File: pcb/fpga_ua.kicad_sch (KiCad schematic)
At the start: 15 parts

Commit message: maybe finished schematic
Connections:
- net FPGA_DEBUG_LED_BLOCK15_1: now reaches U?.C11 (IO_L11P_T1_SRCC_15)
- net FPGA_DEBUG_LED_BLOCK14_1: now reaches U?.R5 (IO_L23P_T3_A03_D19_14)
- no-connect marks 0 -> 39
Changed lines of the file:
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@@
 (kicad_sch (version 20211123) (generator eeschema)
   (paper "A4")
+  (junction (at 74.93 24.13) (diameter 0) (color 0 0 0 0)
+  )
   (junction (at 250.19 31.75) (diameter 0) (color 0 0 0 0)
   )
@@
   (junction (at 222.25 60.96) (diameter 0) (color 0 0 0 0)
   )
-  (junction (at 64.77 30.48) (diameter 0) (color 0 0 0 0)
-  )
-  (junction (at 72.39 30.48) (diameter 0) (color 0 0 0 0)
-  )
-  (junction (at 69.85 30.48) (diameter 0) (color 0 0 0 0)
+  (junction (at 64.77 24.13) (diameter 0) (color 0 0 0 0)
+  )
+  (junction (at 72.39 24.13) (diameter 0) (color 0 0 0 0)
+  )
+  (junction (at 69.85 24.13) (diameter 0) (color 0 0 0 0)
   )
   (junction (at 140.97 30.48) (diameter 0) (color 0 0 0 0)
@@
   (junction (at 143.51 30.48) (diameter 0) (color 0 0 0 0)
   )
-  (junction (at 74.93 30.48) (diameter 0) (color 0 0 0 0)
-  )
   (junction (at 213.36 31.75) (diameter 0) (color 0 0 0 0)
   )
@@
   (junction (at 222.25 24.13) (diameter 0) (color 0 0 0 0)
   )
-  (junction (at 67.31 30.48) (diameter 0) (color 0 0 0 0)
+  (junction (at 67.31 24.13) (diameter 0) (color 0 0 0 0)
   )
   (junction (at 138.43 30.48) (diameter 0) (color 0 0 0 0)
@@
   (junction (at 205.74 53.34) (diameter 0) (color 0 0 0 0)
   )
+  (no_connect (at 153.67 132.08))
+  (no_connect (at 153.67 134.62))
+  (no_connect (at 153.67 137.16))
+  (no_connect (at 153.67 139.7))
+  (no_connect (at 153.67 142.24))
+  (no_connect (at 153.67 144.78))
+  (no_connect (at 153.67 147.32))
+  (no_connect (at 153.67 149.86))
+  (no_connect (at 153.67 152.4))
+  (no_connect (at 153.67 154.94))
+  (no_connect (at 153.67 157.48))
+  (no_connect (at 153.67 50.8))
+  (no_connect (at 153.67 93.98))
+  (no_connect (at 153.67 101.6))
+  (no_connect (at 153.67 106.68))
+  (no_connect (at 153.67 109.22))
+  (no_connect (at 153.67 111.76))
+  (no_connect (at 153.67 114.3))
+  (no_connect (at 153.67 116.84))
+  (no_connect (at 153.67 119.38))
+  (no_connect (at 153.67 121.92))
+  (no_connect (at 153.67 124.46))
+  (no_connect (at 153.67 127))
+  (no_connect (at 52.07 162.56))
+  (no_connect (at 52.07 167.64))
+  (no_connect (at 52.07 170.18))
+  (no_connect (at 52.07 172.72))
+  (no_connect (at 52.07 175.26))
+  (no_connect (at 52.07 104.14))
+  (no_connect (at 52.07 147.32))
+  (no_connect (at 52.07 50.8))
+  (no_connect (at 153.67 175.26))
+  (no_connect (at 153.67 172.72))
+  (no_connect (at 153.67 160.02))
+  (no_connect (at 153.67 162.56))
+  (no_connect (at 153.67 165.1))
+  (no_connect (at 153.67 167.64))
+  (no_connect (at 153.67 170.18))
+  (no_connect (at 153.67 129.54))
   (wire (pts (xy 194.31 53.34) (xy 205.74 53.34))
     (stroke (width 0) (type default) (color 0 0 0 0))
@@
     (stroke (width 0) (type default) (color 0 0 0 0))
   )
+  (wire (pts (xy 74.93 30.48) (xy 74.93 24.13))
+    (stroke (width 0) (type default) (color 0 0 0 0))
+  )
   (wire (pts (xy 138.43 30.48) (xy 140.97 30.48))
     (stroke (width 0) (type default) (color 0 0 0 0))
@@
     (stroke (width 0) (type default) (color 0 0 0 0))
   )
+  (wire (pts (xy 64.77 24.13) (xy 64.77 30.48))
+    (stroke (width 0) (type default) (color 0 0 0 0))
+  )
   (wire (pts (xy 133.35 30.48) (xy 135.89 30.48))
     (stroke (width 0) (type default) (color 0 0 0 0))
   )
-  (wire (pts (xy 67.31 30.48) (xy 69.85 30.48))
-    (stroke (width 0) (type default) (color 0 0 0 0))
-  )
-  (wire (pts (xy 74.93 30.48) (xy 74.93 24.13))
+  (wire (pts (xy 67.31 24.13) (xy 69.85 24.13))
+    (stroke (width 0) (type default) (color 0 0 0 0))
+  )
+  (wire (pts (xy 72.39 24.13) (xy 72.39 30.48))
     (stroke (width 0) (type default) (color 0 0 0 0))
   )
@@
     (stroke (width 0) (type default) (color 0 0 0 0))
   )
+  (wire (pts (xy 69.85 24.13) (xy 69.85 30.48))
+    (stroke (width 0) (type default) (color 0 0 0 0))
+  )
   (wire (pts (xy 231.14 24.13) (xy 222.25 24.13))
     (stroke (width 0) (type default) (color 0 0 0 0))
   )
-  (wire (pts (xy 69.85 30.48) (xy 72.39 30.48))
-    (stroke (width 0) (type default) (color 0 0 0 0))
-  )
-  (wire (pts (xy 72.39 30.48) (xy 74.93 30.48))
+  (wire (pts (xy 69.85 24.13) (xy 72.39 24.13))
+    (stroke (width 0) (type default) (color 0 0 0 0))
+  )
+  (wire (pts (xy 72.39 24.13) (xy 74.93 24.13))
     (stroke (width 0) (type default) (color 0 0 0 0))
   )
@@
     (stroke (width 0) (type default) (color 0 0 0 0))
   )
-  (wire (pts (xy 153.67 104.14) (xy 163.83 104.14))
-    (stroke (width 0) (type default) (color 0 0 0 0))
-  )
   (wire (pts (xy 213.36 60.96) (xy 222.25 60.96))
     (stroke (width 0) (type default) (color 0 0 0 0))
@@
     (stroke (width 0) (type default) (color 0 0 0 0))
   )
-  (wire (pts (xy 64.77 30.48) (xy 67.31 30.48))
-    (stroke (width 0) (type default) (color 0 0 0 0))
-  )
-  (wire (pts (xy 62.23 30.48) (xy 64.77 30.48))
+  (wire (pts (xy 64.77 24.13) (xy 67.31 24.13))
+    (stroke (width 0) (type default) (color 0 0 0 0))
+  )
+  (wire (pts (xy 62.23 24.13) (xy 64.77 24.13))
     (stroke (width 0) (type default) (color 0 0 0 0))
   )
@@
     (stroke (width 0) (type default) (color 0 0 0 0))
   )
+  (wire (pts (xy 62.23 24.13) (xy 62.23 30.48))
+    (stroke (width 0) (type default) (color 0 0 0 0))
+  )
+  (wire (pts (xy 67.31 24.13) (xy 67.31 30.48))
+    (stroke (width 0) (type default) (color 0 0 0 0))
+  )
   (wire (pts (xy 213.36 24.13) (xy 205.74 24.13))
     (stroke (width 0) (type default) (color 0 0 0 0))
@@
     )
   )
+  (global_label "FPGA_DEBUG_LED_BLOCK14_1" (shape input) (at 52.07 165.1 180) (fields_autoplaced)
+    (effects (font (size 1.27 1.27)) (justify right))
+    (property "Intersheet References" "${INTERSHEET_REFS}" (id 0) (at 21.5355 165.0206 0)
+      (effects (font (size 1.27 1.27)) (justify right) hide)
+    )
+  )
   (global_label "SRAM_#CE" (shape bidirectional) (at 52.07 149.86 180) (fields_autoplaced)
     (effects (font (size 1 1)) (justify right))
@@
     (property "Intersheet References" "${INTERSHEET_REFS}" (id 0) (at 160.7605 76.1375 0)
       (effects (font (size 1 1)) (justify left) hide)
+    )
+  )
+  (global_label "FPGA_DEBUG_LED_BLOCK15_1" (shape input) (at 153.67 104.14 0) (fields_autoplaced)
+    (effects (font (size 1.27 1.27)) (justify left))
+    (property "Intersheet References" "${INTERSHEET_REFS}" (id 0) (at 184.2045 104.0606 0)
+      (effects (font (size 1.27 1.27)) (justify left) hide)
     )
   )
@@
   )
   (symbol (lib_id "FPGA_Xilinx_Artix7:XC7A100T-FTG256") (at 102.87 104.14 0) (unit 1)
-    (in_bom yes) (on_board yes) (fields_autoplaced)
-    (property "Reference" "U?" (id 0) (at 104.1401 179.07 90)
+    (in_bom yes) (on_board yes)
+    (property "Reference" "U?" (id 0) (at 107.95 179.07 0)
       (effects (font (size 1.27 1.27)) (justify right))
     )
-    (property "Value" "XC7A100T-FTG256" (id 1) (at 101.6001 179.07 90)
+    (property "Value" "XC7A100T-FTG256" (id 1) (at 101.6001 179.07 0)
       (effects (font (size 1.27 1.27)) (justify right))
     )

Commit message: everything except crystal
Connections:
- net SRAM_D0: now also U?.N13 (IO_L11P_T1_SRCC_14); no longer U?.P13 (IO_L11N_T1_SRCC_14)
- net SRAM_D1: now also U?.P13 (IO_L11N_T1_SRCC_14); no longer U?.N14 (IO_L12P_T1_MRCC_14)
- net SRAM_D2: now also U?.N14 (IO_L12P_T1_MRCC_14); no longer U?.P14 (IO_L12N_T1_MRCC_14)
- net SRAM_D3: now also U?.P14 (IO_L12N_T1_MRCC_14); no longer U?.N11 (IO_L13P_T2_MRCC_14)
- new net Oscillator Clock: U?.N11 (IO_L13P_T2_MRCC_14)

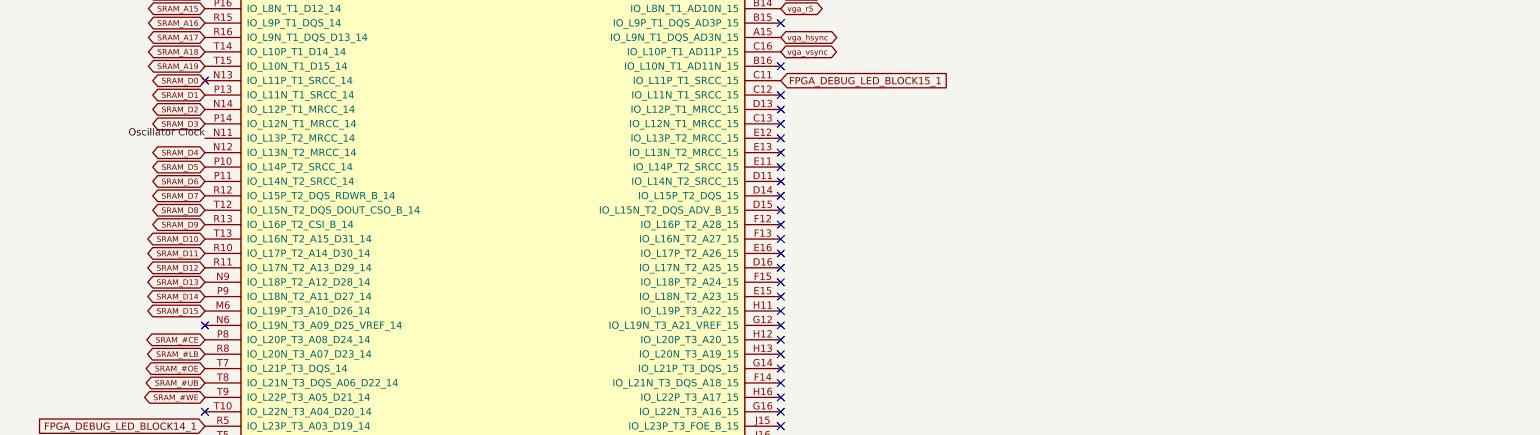
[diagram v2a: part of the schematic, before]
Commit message: add oscilattor + spi debug+ cap on sramd
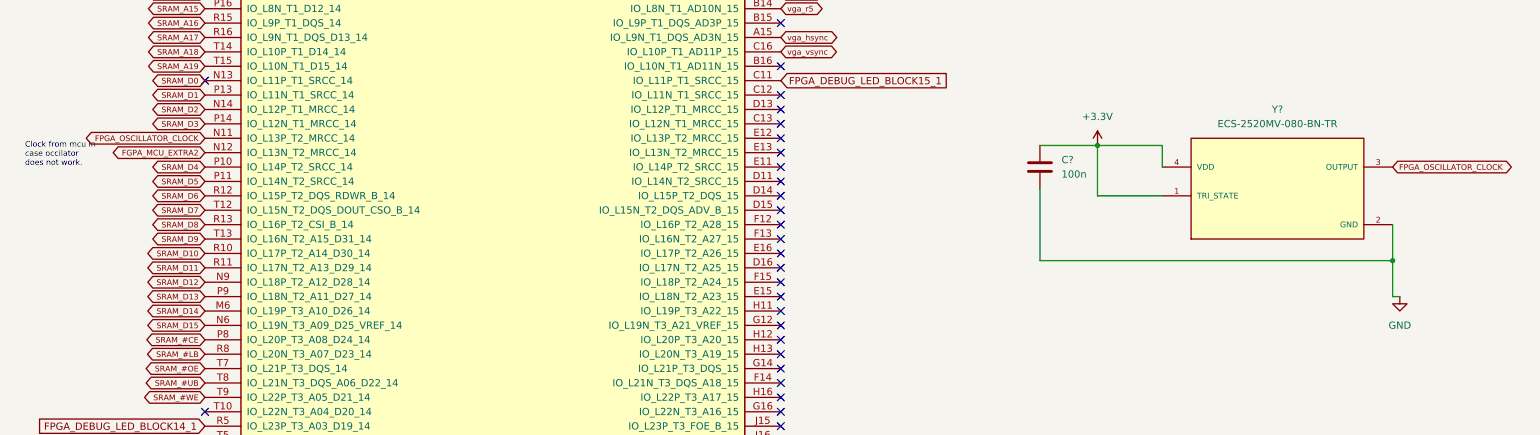
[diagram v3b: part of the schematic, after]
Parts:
- added C?: 100n, symbol Device:C
- added Y?: ECS-2520MV-080-BN-TR, oscillator-footprints:OSC_ECS-2520S25-250-FN-TR, symbol ECS-2520MV-080-BN-TR:ECS-2520MV-080-BN-TR
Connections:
- net GND: now also C?.2, Y?.2 (GND)
- net SRAM_D10: now also U?.R10 (IO_L17P_T2_A14_D30_14); no longer U?.T13 (IO_L16N_T2_A15_D31_14)
- net SRAM_D11: now also U?.R11 (IO_L17N_T2_A13_D29_14); no longer U?.R10 (IO_L17P_T2_A14_D30_14)
- net SRAM_D12: now also U?.N9 (IO_L18P_T2_A12_D28_14); no longer U?.R11 (IO_L17N_T2_A13_D29_14)
- net SRAM_D13: now also U?.P9 (IO_L18N_T2_A11_D27_14); no longer U?.N9 (IO_L18P_T2_A12_D28_14)
- net SRAM_D14: now also U?.M6 (IO_L19P_T3_A10_D26_14); no longer U?.P9 (IO_L18N_T2_A11_D27_14)
- net SRAM_D15: now also U?.N6 (IO_L19N_T3_A09_D25_VREF_14); no longer U?.M6 (IO_L19P_T3_A10_D26_14)
- net SRAM_D4: now also U?.P10 (IO_L14P_T2_SRCC_14); no longer U?.N12 (IO_L13N_T2_MRCC_14)
- net SRAM_D5: now also U?.P11 (IO_L14N_T2_SRCC_14); no longer U?.P10 (IO_L14P_T2_SRCC_14)
- net SRAM_D6: now also U?.R12 (IO_L15P_T2_DQS_RDWR_B_14); no longer U?.P11 (IO_L14N_T2_SRCC_14)
- net SRAM_D7: now also U?.T12 (IO_L15N_T2_DQS_DOUT_CSO_B_14); no longer U?.R12 (IO_L15P_T2_DQS_RDWR_B_14)
- net SRAM_D8: now also U?.R13 (IO_L16P_T2_CSI_B_14); no longer U?.T12 (IO_L15N_T2_DQS_DOUT_CSO_B_14)
- net SRAM_D9: now also U?.T13 (IO_L16N_T2_A15_D31_14); no longer U?.R13 (IO_L16P_T2_CSI_B_14)
- net Oscillator Clock renamed FPGA_OSCILLATOR_CLOCK
- net FPGA_OSCILLATOR_CLOCK: now also Y?.3 (OUTPUT)
- new net +3.3V: C?.1, Y?.1 (TRI_STATE), Y?.4 (VDD)
- new net FGPA_MCU_EXTRA2: U?.N12 (IO_L13N_T2_MRCC_14)
- no-connect marks 39 -> 38
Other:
- note added: "Clock from mcu in case occilator does not work."

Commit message: add footprints
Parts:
- C1101: renamed from C?; footprint (none) -> Capacitor_SMD:C_0603_1608Metric_Pad1.08x0.95mm_HandSolder
- U1101: renamed from U?; footprint (none) -> fpga:BGA256C100P16X16_1700X1700X155
- gave numbers to parts that had none: 15
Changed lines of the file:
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@@
   (symbol (lib_id "Device:C") (at 205.74 27.94 0) (unit 1)
     (in_bom yes) (on_board yes)
-    (property "Reference" "C?" (id 0) (at 206.375 25.4 0)
+    (property "Reference" "C1102" (id 0) (at 206.375 25.4 0)
       (effects (font (size 1.27 1.27)) (justify left))
     )
@@
   (symbol (lib_id "power:GND") (at 267.97 31.75 0) (unit 1)
     (in_bom yes) (on_board yes)
-    (property "Reference" "#PWR?" (id 0) (at 267.97 38.1 0)
+    (property "Reference" "#PWR01104" (id 0) (at 267.97 38.1 0)
       (effects (font (size 1.27 1.27)) hide)
     )
@@
   (symbol (lib_id "Device:C") (at 259.08 27.94 0) (unit 1)
     (in_bom yes) (on_board yes)
-    (property "Reference" "C?" (id 0) (at 259.715 25.4 0)
+    (property "Reference" "C1114" (id 0) (at 259.715 25.4 0)
       (effects (font (size 1.27 1.27)) (justify left))
     )
@@
   (symbol (lib_id "Device:C") (at 222.25 27.94 0) (unit 1)
     (in_bom yes) (on_board yes)
-    (property "Reference" "C?" (id 0) (at 222.885 25.4 0)
+    (property "Reference" "C1106" (id 0) (at 222.885 25.4 0)
       (effects (font (size 1.27 1.27)) (justify left))
     )
@@
   (symbol (lib_id "FPGA_Xilinx_Artix7:XC7A100T-FTG256") (at 102.87 104.14 0) (unit 1)
     (in_bom yes) (on_board yes)
-    (property "Reference" "U?" (id 0) (at 107.95 179.07 0)
+    (property "Reference" "U1101" (id 0) (at 111.76 179.07 0)
       (effects (font (size 1.27 1.27)) (justify right))
     )
@@
       (effects (font (size 1.27 1.27)) (justify right))
     )
-    (property "Footprint" "" (id 2) (at 102.87 104.14 0)
+    (property "Footprint" "fpga:BGA256C100P16X16_1700X1700X155" (id 2) (at 102.87 104.14 0)
       (effects (font (size 1.27 1.27)) hide)
     )
@@
   (symbol (lib_id "power:+3.3V") (at 209.55 115.57 0) (unit 1)
     (in_bom yes) (on_board yes) (fields_autoplaced)
-    (property "Reference" "#PWR?" (id 0) (at 209.55 119.38 0)
+    (property "Reference" "#PWR01101" (id 0) (at 209.55 119.38 0)
       (effects (font (size 1.27 1.27)) hide)
     )
@@
   (symbol (lib_id "Device:C") (at 231.14 27.94 0) (unit 1)
     (in_bom yes) (on_board yes)
-    (property "Reference" "C?" (id 0) (at 231.775 25.4 0)
+    (property "Reference" "C1108" (id 0) (at 231.775 25.4 0)
       (effects (font (size 1.27 1.27)) (justify left))
     )
@@
   (symbol (lib_id "Device:C") (at 240.03 57.15 0) (unit 1)
     (in_bom yes) (on_board yes)
-    (property "Reference" "C?" (id 0) (at 240.665 54.61 0)
+    (property "Reference" "C1111" (id 0) (at 240.665 54.61 0)
       (effects (font (size 1.27 1.27)) (justify left))
     )
@@
   (symbol (lib_id "Device:C") (at 250.19 57.15 0) (unit 1)
     (in_bom yes) (on_board yes)
-    (property "Reference" "C?" (id 0) (at 250.825 54.61 0)
+    (property "Reference" "C1113" (id 0) (at 250.825 54.61 0)
       (effects (font (size 1.27 1.27)) (justify left))
     )
@@
   (symbol (lib_id "Device:C") (at 199.39 119.38 0) (unit 1)
     (in_bom yes) (on_board yes) (fields_autoplaced)
-    (property "Reference" "C?" (id 0) (at 203.2 118.1099 0)
+    (property "Reference" "C1101" (id 0) (at 203.2 118.1099 0)
       (effects (font (size 1.27 1.27)) (justify left))
     )
@@
       (effects (font (size 1.27 1.27)) (justify left))
     )
-    (property "Footprint" "" (id 2) (at 200.3552 123.19 0)
+    (property "Footprint" "Capacitor_SMD:C_0603_1608Metric_Pad1.08x0.95mm_HandSolder" (id 2) (at 200.3552 123.19 0)
       (effects (font (size 1.27 1.27)) hide)
     )
@@
   (symbol (lib_id "Device:C") (at 240.03 27.94 0) (unit 1)
     (in_bom yes) (on_board yes)
-    (property "Reference" "C?" (id 0) (at 240.665 25.4 0)
+    (property "Reference" "C1110" (id 0) (at 240.665 25.4 0)
       (effects (font (size 1.27 1.27)) (justify left))
     )
@@
   (symbol (lib_id "Device:C") (at 222.25 57.15 0) (unit 1)
     (in_bom yes) (on_board yes)
-    (property "Reference" "C?" (id 0) (at 222.885 54.61 0)
+    (property "Reference" "C1107" (id 0) (at 222.885 54.61 0)
       (effects (font (size 1.27 1.27)) (justify left))
     )
@@
   (symbol (lib_id "power:GND") (at 267.97 60.96 0) (unit 1)
     (in_bom yes) (on_board yes)
-    (property "Reference" "#PWR?" (id 0) (at 267.97 67.31 0)
+    (property "Reference" "#PWR01106" (id 0) (at 267.97 67.31 0)
       (effects (font (size 1.27 1.27)) hide)
     )
@@
   (symbol (lib_id "Device:C") (at 250.19 27.94 0) (unit 1)
     (in_bom yes) (on_board yes)
-    (property "Reference" "C?" (id 0) (at 250.825 25.4 0)
+    (property "Reference" "C1112" (id 0) (at 250.825 25.4 0)
       (effects (font (size 1.27 1.27)) (justify left))
     )
@@
   (symbol (lib_id "Device:C") (at 231.14 57.15 0) (unit 1)
     (in_bom yes) (on_board yes)
-    (property "Reference" "C?" (id 0) (at 231.775 54.61 0)
+    (property "Reference" "C1109" (id 0) (at 231.775 54.61 0)
       (effects (font (size 1.27 1.27)) (justify left))
     )
@@
   (symbol (lib_id "Device:C") (at 259.08 57.15 0) (unit 1)
     (in_bom yes) (on_board yes)
-    (property "Reference" "C?" (id 0) (at 259.715 54.61 0)
+    (property "Reference" "C1115" (id 0) (at 259.715 54.61 0)
       (effects (font (size 1.27 1.27)) (justify left))
     )
@@
   (symbol (lib_id "power:+3V3") (at 267.97 24.13 0) (unit 1)
     (in_bom yes) (on_board yes)
-    (property "Reference" "#PWR?" (id 0) (at 267.97 27.94 0)
+    (property "Reference" "#PWR01103" (id 0) (at 267.97 27.94 0)
       (effects (font (size 1.27 1.27)) hide)
     )
@@
   (symbol (lib_id "Device:C") (at 213.36 27.94 0) (unit 1)
     (in_bom yes) (on_board yes)
-    (property "Reference" "C?" (id 0) (at 213.995 25.4 0)
+    (property "Reference" "C1104" (id 0) (at 213.995 25.4 0)
       (effects (font (size 1.27 1.27)) (justify left))
     )
@@
   (symbol (lib_id "Device:C") (at 213.36 57.15 0) (unit 1)
     (in_bom yes) (on_board yes)
-    (property "Reference" "C?" (id 0) (at 213.995 54.61 0)
+    (property "Reference" "C1105" (id 0) (at 213.995 54.61 0)
       (effects (font (size 1.27 1.27)) (justify left))
     )
@@
   (symbol (lib_id "ECS-2520MV-080-BN-TR:ECS-2520MV-080-BN-TR") (at 241.3 121.92 0) (unit 1)
     (in_bom yes) (on_board yes) (fields_autoplaced)
-    (property "Reference" "Y?" (id 0) (at 241.3 109.22 0))
+    (property "Reference" "Y1101" (id 0) (at 241.3 109.22 0))
     (property "Value" "ECS-2520MV-080-BN-TR" (id 1) (at 241.3 111.76 0))
     (property "Footprint" "oscillator-footprints:OSC_ECS-2520S25-250-FN-TR" (id 2) (at 241.3 121.92 0)
@@
   (symbol (lib_id "power:+3V3") (at 267.97 53.34 0) (unit 1)
     (in_bom yes) (on_board yes)
-    (property "Reference" "#PWR?" (id 0) (at 267.97 57.15 0)
+    (property "Reference" "#PWR01105" (id 0) (at 267.97 57.15 0)
       (effects (font (size 1.27 1.27)) hide)
     )
@@
   (symbol (lib_id "Device:C") (at 205.74 57.15 0) (unit 1)
     (in_bom yes) (on_board yes)
-    (property "Reference" "C?" (id 0) (at 206.375 54.61 0)
+    (property "Reference" "C1103" (id 0) (at 206.375 54.61 0)
       (effects (font (size 1.27 1.27)) (justify left))
     )
@@
   (symbol (lib_id "power:GND") (at 262.89 142.24 0) (unit 1)
     (in_bom yes) (on_board yes) (fields_autoplaced)
-    (property "Reference" "#PWR?" (id 0) (at 262.89 148.59 0)
-      (effects (font (size 1.27 1.27)) hide)
-    )
+    (property "Reference" "#PWR01102" (id 0) (at 262.89 148.59 0)
+      (effects (font (size 1.27 1.27)) hide)
+    )
